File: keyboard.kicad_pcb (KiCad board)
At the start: 2 copper layers, 129 parts, among them U1 MOUDLE-SEEEDUINO-XIAO

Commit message: Got everything placed
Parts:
- removed D67, D68, D69, D70: D0-35, onesemi-1N914:ON_Semiconductor-017AG-08_2016-O-MFG
- removed U1: MOUDLE-SEEEDUINO-XIAO, XIAO_PCB:MOUDLE14P-2.54-21X17.8MM
- added D60: D0-35, onesemi-1N914:ON_Semiconductor-017AG-08_2016-O-MFG, F.Cu at (319.1, 73.8)
- added D61: D0-35, onesemi-1N914:ON_Semiconductor-017AG-08_2016-O-MFG, F.Cu at (322.3, 73.8)
- added D62: DO-35, onesemi-1N914:ON_Semiconductor-017AG-08_2016-O-MFG, F.Cu at (269.1, 65.9)
- added D64: D0-35, onesemi-1N914:ON_Semiconductor-017AG-08_2016-O-MFG, F.Cu at (319.1, 65.9)
- D1: footprint onesemi-1N914:ON_Semiconductor-017AG-08_2016-O-MFG -> MCU_RaspberryPi_and_Boards:RPi_Pico_SMD_TH; moved to B.Cu
- D55: value DO-35 -> D0-35
- locked: renamed from ENC1; value PEC11L-4120K-S0020 -> locked
- locked: renamed from ENC3; value PEC11L-4120K-S0020 -> locked
- locked: renamed from ENC2; value PEC11L-4120K-S0020 -> locked
- moved D2 435.6 mm to (61.9, 73.8), turned to -90 degrees
- moved D3 432.6 mm to (65.1, 73.8), turned to -90 degrees
- moved D4 429.6 mm to (68.3, 73.8), turned to -90 degrees
- moved D5 426.6 mm to (71.4, 73.8), turned to -90 degrees
- moved D6 422.1 mm to (76.2, 73.8), turned to -90 degrees
- moved D7 419.2 mm to (79.4, 73.8), turned to -90 degrees
- moved D8 416.3 mm to (82.5, 73.8), turned to -90 degrees
- moved D9 411.9 mm to (87.3, 73.8), turned to -90 degrees
- moved D10 409.0 mm to (90.5, 73.8), turned to -90 degrees
- moved D11 406.2 mm to (93.7, 73.8), turned to -90 degrees
- moved D12 403.4 mm to (96.8, 73.8), turned to -90 degrees
- moved D13 400.7 mm to (100.0, 73.8), turned to -90 degrees
- moved D14 396.4 mm to (104.8, 73.8), turned to -90 degrees
- moved D15 393.7 mm to (108.0, 73.8), turned to -90 degrees
- moved D17 393.2 mm to (114.3, 73.8), turned to -90 degrees
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- renumbered MX42 to MX41, MX43 to MX42, MX45 to MX43, MX46 to MX44, MX47 to MX45, MX48 to MX46, MX49 to MX47, MX50 to MX48, MX51 to MX49, MX52 to MX50, MX53 to MX51, MX54 to MX52, MX56 to MX53, MX57 to MX54, MX58 to MX55, MX59 to MX56, MX63 to MX57, MX67 to MX58, MX68 to MX59, MX69 to MX60, MX70 to MX61
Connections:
- D10 pad 1: ROW0 -> ROW1
- D11 pad 1: ROW0 -> Net-(D11-K)
- D12 pad 1: ROW0 -> ROW3
- D13 pad 1: ROW0 -> ROW4
- D16 pad 1: ROW1 -> Net-(D11-K)
- D17 pad 1: ROW1 -> ROW3
- D18 pad 1: ROW1 -> ROW0
- D2 pad 1: ROW0 -> ROW1
- D20 pad 1: ROW1 -> Net-(D11-K)
- D21 pad 1: ROW1 -> ROW3
- D22 pad 1: ROW1 -> ROW0
- D24 pad 1: ROW1 -> Net-(D11-K)
- D25 pad 1: ROW1 -> ROW3
- D26 pad 1: ROW1 -> ROW0
- D28 pad 1: ROW1 -> Net-(D11-K)
- D29 pad 1: ROW2 -> ROW3
- D3 pad 1: ROW0 -> ROW2
- D30 pad 1: ROW2 -> ROW0
- D31 pad 1: ROW2 -> ROW1
- D32 pad 1: ROW2 -> Net-(D11-K)
- D33 pad 1: ROW2 -> ROW3
- D34 pad 1: ROW2 -> ROW4
- D35 pad 1: ROW2 -> ROW0
- D36 pad 1: ROW2 -> ROW1
- D37 pad 1: ROW2 -> Net-(D11-K)
- D38 pad 1: ROW2 -> ROW3
- D39 pad 1: ROW2 -> ROW0
- D4 pad 1: ROW0 -> ROW3
- D40 pad 1: ROW2 -> ROW1
- D41 pad 1: ROW0 -> Net-(D11-K)
- D42 pad 1: ROW2 -> ROW3
- D43 pad 1: ROW3 -> ROW0
- D44 pad 1: ROW0 -> ROW1
- D45 pad 1: ROW3 -> Net-(D11-K)
- D47 pad 1: ROW3 -> ROW4
- D48 pad 1: ROW3 -> ROW0
- D49 pad 1: ROW3 -> ROW1
- D5 pad 1: ROW0 -> ROW4
- D50 pad 1: ROW3 -> Net-(D11-K)
- D52 pad 1: ROW3 -> ROW4
- D53 pad 1: ROW3 -> ROW0
- D54 pad 1: ROW3 -> ROW1
- D55 pad 1: ROW0 -> Net-(D11-K)
- D56 pad 1: ROW3 -> ROW4
- D57 pad 1: ROW4 -> ROW0
- D58 pad 1: ROW4 -> ROW1
- D59 pad 1: ROW4 -> Net-(D11-K)
- D63 pad 1: ROW4 -> ROW0
- D7 pad 1: ROW0 -> ROW1
- D8 pad 1: ROW0 -> ROW4
- MX10 pad 2: Net-(D10-A) -> Net-(D39-A)
- MX11 pad 2: Net-(D11-A) -> Net-(D43-A)
- MX12 pad 2: Net-(D12-A) -> Net-(D48-A)
- MX13 pad 2: Net-(D13-A) -> Net-(D53-A)
- MX14 pad 2: Net-(D14-A) -> Net-(D57-A)
- MX15 pad 2: Net-(D15-A) -> Net-(D2-A)
- MX16 pad 2: Net-(D16-A) -> Net-(D7-A)
- MX17 pad 2: Net-(D17-A) -> Net-(D10-A)
- MX18 pad 2: Net-(D18-A) -> Net-(D15-A)
- MX2 pad 2: Net-(D2-A) -> Net-(D6-A)
- MX20 pad 2: Net-(D20-A) -> Net-(D23-A)
- MX21 pad 2: Net-(D21-A) -> Net-(D27-A)
- MX22 pad 2: Net-(D22-A) -> Net-(D31-A)
- MX23 pad 2: Net-(D23-A) -> Net-(D36-A)
- MX24 pad 2: Net-(D24-A) -> Net-(D40-A)
- MX25 pad 2: Net-(D25-A) -> Net-(D44-A)
- MX26 pad 2: Net-(D26-A) -> Net-(D49-A)
- MX27 pad 2: Net-(D27-A) -> Net-(D54-A)
- MX28 pad 2: Net-(D28-A) -> Net-(D58-A)
- MX29 pad 2: Net-(D29-A) -> Net-(D3-A)
- MX3 pad 2: Net-(D3-A) -> Net-(D9-A)
- MX30 pad 1: COL1 -> COL2
- MX30 pad 2: Net-(D30-A) -> Net-(D11-A)
- MX31 pad 2: Net-(D31-A) -> Net-(D16-A)
- MX32 pad 2: Net-(D32-A) -> Net-(D20-A)
- MX33 pad 2: Net-(D33-A) -> Net-(D24-A)
- MX34 pad 2: Net-(D34-A) -> Net-(D28-A)
- MX35 pad 2: Net-(D35-A) -> Net-(D32-A)
- MX36 pad 2: Net-(D36-A) -> Net-(D37-A)
- MX37 pad 2: Net-(D37-A) -> Net-(D41-A)
- MX38 pad 2: Net-(D38-A) -> Net-(D45-A)
- MX39 pad 2: Net-(D39-A) -> Net-(D50-A)
- MX4 pad 2: Net-(D4-A) -> Net-(D14-A)
- MX40 pad 1: ROW1 -> COL12
- MX40 pad 2: Net-(D40-A) -> Net-(D55-A)
- MX41 pad 2: Net-(D42-A) -> Net-(D59-A)
- MX42 pad 2: Net-(D43-A) -> Net-(D4-A)
- MX43 pad 1: COl3 -> COL2
- MX43 pad 2: Net-(D45-A) -> Net-(D12-A)
- MX44 pad 1: COl4 -> COl3
- MX44 pad 2: Net-(D46-A) -> Net-(D17-A)
- MX45 pad 1: COL5 -> COl4
- MX45 pad 2: Net-(D47-A) -> Net-(D21-A)
- MX46 pad 1: COL6 -> COL5
- MX46 pad 2: Net-(D48-A) -> Net-(D25-A)
- MX47 pad 1: COL7 -> COL6
- MX47 pad 2: Net-(D49-A) -> Net-(D29-A)
- MX48 pad 1: COL8 -> COL7
- MX48 pad 2: Net-(D50-A) -> Net-(D33-A)
- MX49 pad 1: COL9 -> COL8
- MX49 pad 2: Net-(D51-A) -> Net-(D38-A)
- MX5 pad 2: Net-(D5-A) -> Net-(D18-A)
- MX50 pad 1: COL10 -> COL9
- MX50 pad 2: Net-(D52-A) -> Net-(D42-A)
- MX51 pad 1: COL11 -> COL10
- MX51 pad 2: Net-(D53-A) -> Net-(D46-A)
- MX52 pad 1: ROW2 -> COL11
- MX52 pad 2: Net-(D54-A) -> Net-(D51-A)
- MX53 pad 2: Net-(D56-A) -> Net-(D60-A)
- MX54 pad 2: Net-(D57-A) -> Net-(D5-A)
- MX55 pad 2: Net-(D58-A) -> Net-(D8-A)
- MX56 pad 2: Net-(D59-A) -> Net-(D13-A)
- MX57 pad 1: COL8 -> COL7
- MX57 pad 2: Net-(D63-A) -> Net-(D34-A)
- MX58 pad 2: Net-(D67-A) -> Net-(D47-A)
- MX59 pad 2: Net-(D68-A) -> Net-(D52-A)
- MX6 pad 2: Net-(D6-A) -> Net-(D22-A)
- MX60 pad 1: ROW2 -> COL12
- MX60 pad 2: Net-(D69-A) -> Net-(D56-A)
- MX7 pad 2: Net-(D7-A) -> Net-(D26-A)
- MX8 pad 2: Net-(D8-A) -> Net-(D30-A)
- MX9 pad 2: Net-(D9-A) -> Net-(D35-A)
- locked pad 2: Net-(D41-A) -> Net-(D64-A)
- locked pad 1: COL10 -> COL11
- locked pad 2: Net-(D55-A) -> Net-(D62-A)
- locked pad 2: Net-(D44-A) -> Net-(D63-A)
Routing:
- net COL7: track 0.00 -> 93.9 mm
- net Net-(D5-A): track 0.00 -> 92.9 mm
- net COL12: track 0.00 -> 92.1 mm
- net COl3: track 0.00 -> 90.9 mm
- net Net-(D8-A): track 0.00 -> 89.1 mm
- net COL11: track 0.00 -> 87.2 mm
- net COL10: track 0.00 -> 86.1 mm
- net COL13: track 0.00 -> 84.1 mm
- net COL0: track 0.00 -> 83.1 mm
- net COL1: track 0.00 -> 81.9 mm
- net COl4: track 0.00 -> 69.0 mm
- net COL5: track 0.00 -> 69.0 mm
- net COL6: track 0.00 -> 69.0 mm
- net COL2: track 0.00 -> 69.0 mm
- net COL9: track 0.00 -> 68.0 mm
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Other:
- board outline added: 285.8 x 125.4 mm

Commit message: forgot to save
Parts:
- added U1: Pi Pico, MCU_RaspberryPi_and_Boards:RPi_Pico_SMD_TH, B.Cu at (198.4, 75.4)
- D1: value D0-35 -> DO-35; footprint MCU_RaspberryPi_and_Boards:RPi_Pico_SMD_TH -> onesemi-1N914:ON_Semiconductor-017AG-08_2016-O-MFG; moved to F.Cu
- moved D1 139.7 mm to (58.7, 73.8), turned to -90 degrees

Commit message: Routed diodes to switches
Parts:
- D1: value DO-35 -> PI Pico
- U1: value Pi Pico -> Pico
- moved D17 14.3 mm to (114.3, 73.8)
- moved D13 3.18 mm to (101.6, 73.8)
- moved D14 3.17 mm to (104.8, 73.8)
- moved D15 3.17 mm to (108.0, 73.8)
- moved D16 3.17 mm to (111.1, 73.8)
- renumbered D14 to D13, D15 to D14, D16 to D15, D17 to D16, D13 to D17
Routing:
- net Net-(D34-A): track 0.00 -> 132.6 mm
- net Net-(D52-A): track 0.00 -> 113.2 mm
- net Net-(D17-A): track 0.00 -> 111.6 mm
- net Net-(D47-A): track 0.00 -> 110.8 mm
- net Net-(D33-A): track 0.00 -> 109.6 mm
- net Net-(D56-A): track 0.00 -> 102.5 mm
- net Net-(D29-A): track 0.00 -> 100.6 mm
- net Net-(D32-A): track 0.00 -> 96.6 mm
- net Net-(D61-A): track 0.00 -> 95.2 mm
- net Net-(D37-A): track 0.00 -> 93.9 mm
- net Net-(D25-A): track 0.00 -> 93.8 mm
- net Net-(D51-A): track 0.00 -> 93.6 mm
- net Net-(D46-A): track 0.00 -> 91.9 mm
- net Net-(D21-A): track 0.00 -> 90.5 mm
- net Net-(D16-A): track 0.00 -> 89.1 mm
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
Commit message: Tracing mostly done just do DRC
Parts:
- D2: moved to B.Cu
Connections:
- D11 pad 1: Net-(D11-K) -> ROW2
- D15 pad 1: Net-(D11-K) -> ROW2
- D20 pad 1: Net-(D11-K) -> ROW2
- D24 pad 1: Net-(D11-K) -> ROW2
- D28 pad 1: Net-(D11-K) -> ROW2
- D32 pad 1: Net-(D11-K) -> ROW2
- D37 pad 1: Net-(D11-K) -> ROW2
- D41 pad 1: Net-(D11-K) -> ROW2
- D45 pad 1: Net-(D11-K) -> ROW2
- D50 pad 1: Net-(D11-K) -> ROW2
- D55 pad 1: Net-(D11-K) -> ROW2
- D59 pad 1: Net-(D11-K) -> ROW2
- MX18 pad 1: COl3 -> COL3
- MX19 pad 1: COl4 -> COL4
- MX31 pad 1: COl3 -> COL3
- MX32 pad 1: COl4 -> COL4
- MX4 pad 1: COl3 -> COL3
- MX44 pad 1: COl3 -> COL3
- MX45 pad 1: COl4 -> COL4
- MX5 pad 1: COl4 -> COL4
- MX56 pad 1: COl3 -> COL3
- U1 pad 1: unconnected-(U1-GPIO0-Pad1) -> ENC3B
- U1 pad 10: unconnected-(U1-GPIO7-Pad10) -> ENC2A
- U1 pad 11: unconnected-(U1-GPIO8-Pad11) -> ENC1B
- U1 pad 12: unconnected-(U1-GPIO9-Pad12) -> ENC1A
- U1 pad 13: unconnected-(U1-GND-Pad13) -> GND
- U1 pad 14: unconnected-(U1-GPIO10-Pad14) -> COL8
- U1 pad 15: unconnected-(U1-GPIO11-Pad15) -> COL9
- U1 pad 16: unconnected-(U1-GPIO12-Pad16) -> COL10
- U1 pad 17: unconnected-(U1-GPIO13-Pad17) -> COL11
- U1 pad 18: unconnected-(U1-GND-Pad18) -> GND
- U1 pad 19: unconnected-(U1-GPIO14-Pad19) -> COL12
- U1 pad 2: unconnected-(U1-GPIO1-Pad2) -> ENC3A
- U1 pad 20: unconnected-(U1-GPIO15-Pad20) -> COL13
- U1 pad 21: unconnected-(U1-GPIO16-Pad21) -> COL2
- U1 pad 22: unconnected-(U1-GPIO17-Pad22) -> COL3
- U1 pad 23: unconnected-(U1-GND-Pad23) -> GND
- U1 pad 24: unconnected-(U1-GPIO18-Pad24) -> COL4
- U1 pad 25: unconnected-(U1-GPIO19-Pad25) -> COL5
- U1 pad 26: unconnected-(U1-GPIO20-Pad26) -> COL6
- U1 pad 27: unconnected-(U1-GPIO21-Pad27) -> COL7
- U1 pad 28: unconnected-(U1-GND-Pad28) -> GND
- U1 pad 29: unconnected-(U1-GPIO22-Pad29) -> COL1
- U1 pad 3: unconnected-(U1-GND-Pad3) -> GND
- U1 pad 31: unconnected-(U1-GPIO26_ADC0-Pad31) -> COL0
- U1 pad 34: unconnected-(U1-GPIO28_ADC2-Pad34) -> ROW0
- U1 pad 38: unconnected-(U1-GND-Pad38) -> GND
- U1 pad 4: unconnected-(U1-GPIO2-Pad4) -> ROW4
- U1 pad 5: unconnected-(U1-GPIO3-Pad5) -> ROW3
- U1 pad 6: unconnected-(U1-GPIO4-Pad6) -> ROW2
- U1 pad 7: unconnected-(U1-GPIO5-Pad7) -> ROW1
- U1 pad 8: unconnected-(U1-GND-Pad8) -> GND
- U1 pad 9: unconnected-(U1-GPIO6-Pad9) -> ENC2B
- locked pad A: unconnected-(ENC3-CHANNEL_A-PadA) -> ENC3A
- locked pad B: unconnected-(ENC3-CHANNEL_B-PadB) -> ENC3B
- locked pad C: unconnected-(ENC3-COMMON-PadC) -> GND
- locked pad A: unconnected-(ENC1-CHANNEL_A-PadA) -> ENC1A
- locked pad B: unconnected-(ENC1-CHANNEL_B-PadB) -> ENC1B
- locked pad C: unconnected-(ENC1-COMMON-PadC) -> GND
- locked pad A: unconnected-(ENC2-CHANNEL_A-PadA) -> ENC2A
- locked pad B: unconnected-(ENC2-CHANNEL_B-PadB) -> ENC2B
- locked pad C: unconnected-(ENC2-COMMON-PadC) -> GND
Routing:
- net ROW3: track 0.00 -> 319.1 mm, vias 0 -> 12
- net ROW2: track 0.00 -> 313.6 mm, vias 0 -> 12
- net ROW4: track 0.00 -> 313.3 mm, vias 0 -> 8
- net ROW0: track 0.00 -> 288.4 mm, vias 0 -> 3
- net ROW1: track 0.00 -> 275.2 mm, vias 0 -> 13
- net GND: track 0.00 -> 171.9 mm, vias 0 -> 6
- net COL3: track 0.00 -> 166.5 mm
- net ENC3B: track 0.00 -> 149.4 mm
- net ENC3A: track 0.00 -> 146.7 mm
- net COL0: track 83.1 -> 214.8 mm
- net ENC2A: track 0.00 -> 128.3 mm
- net ENC2B: track 0.00 -> 128.2 mm
- net COL4: track 0.00 -> 123.3 mm
- net COL13: track 109.3 -> 225.9 mm
- net COL1: track 81.9 -> 192.1 mm
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
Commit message: Should be completely done
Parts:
- added ?: , , F.Cu at (95.2, 93.7)
- added REF**: MountingHoleM2-5mmby2mm, MountingHoles:MountingHoleM2-5mmby2mm, F.Cu at (83.3, 108.0)
- added REF**: MountingHoleM2-5mmby2mm, MountingHoles:MountingHoleM2-5mmby2mm, F.Cu at (315.1, 108.0)
- added REF**: MountingHoleM2-5mmby2mm, MountingHoles:MountingHoleM2-5mmby2mm, F.Cu at (95.2, 93.7)
- added REF**: MountingHoleM2-5mmby2mm, MountingHoles:MountingHoleM2-5mmby2mm, F.Cu at (304.8, 91.3)
- added REF**: MountingHoleM2-5mmby2mm, MountingHoles:MountingHoleM2-5mmby2mm, F.Cu at (96.8, 146.1)
- added REF**: MountingHoleM2-5mmby2mm, MountingHoles:MountingHoleM2-5mmby2mm, F.Cu at (191.3, 115.9)
- added REF**: MountingHoleM2-5mmby2mm, MountingHoles:MountingHoleM2-5mmby2mm, F.Cu at (293.7, 146.1)
- D2: moved to F.Cu
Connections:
- U1 pad 13: GND -> unconnected-(U1-GND-Pad13)
- U1 pad 23: GND -> unconnected-(U1-GND-Pad23)
- U1 pad 28: GND -> unconnected-(U1-GND-Pad28)
- U1 pad 3: GND -> unconnected-(U1-GND-Pad3)
- U1 pad 38: GND -> unconnected-(U1-GND-Pad38)
- U1 pad 8: GND -> unconnected-(U1-GND-Pad8)
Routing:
- net ROW2: track 313.6 -> 318.1 mm, vias 12 -> 13
- net ROW1: track 275.2 -> 278.1 mm, vias 13 -> 14
- net ROW0: track 288.4 -> 290.1 mm
- net COL10: track 135.0 -> 133.9 mm
- net GND: track 171.9 -> 172.9 mm
- net COL12: track 208.1 -> 207.2 mm

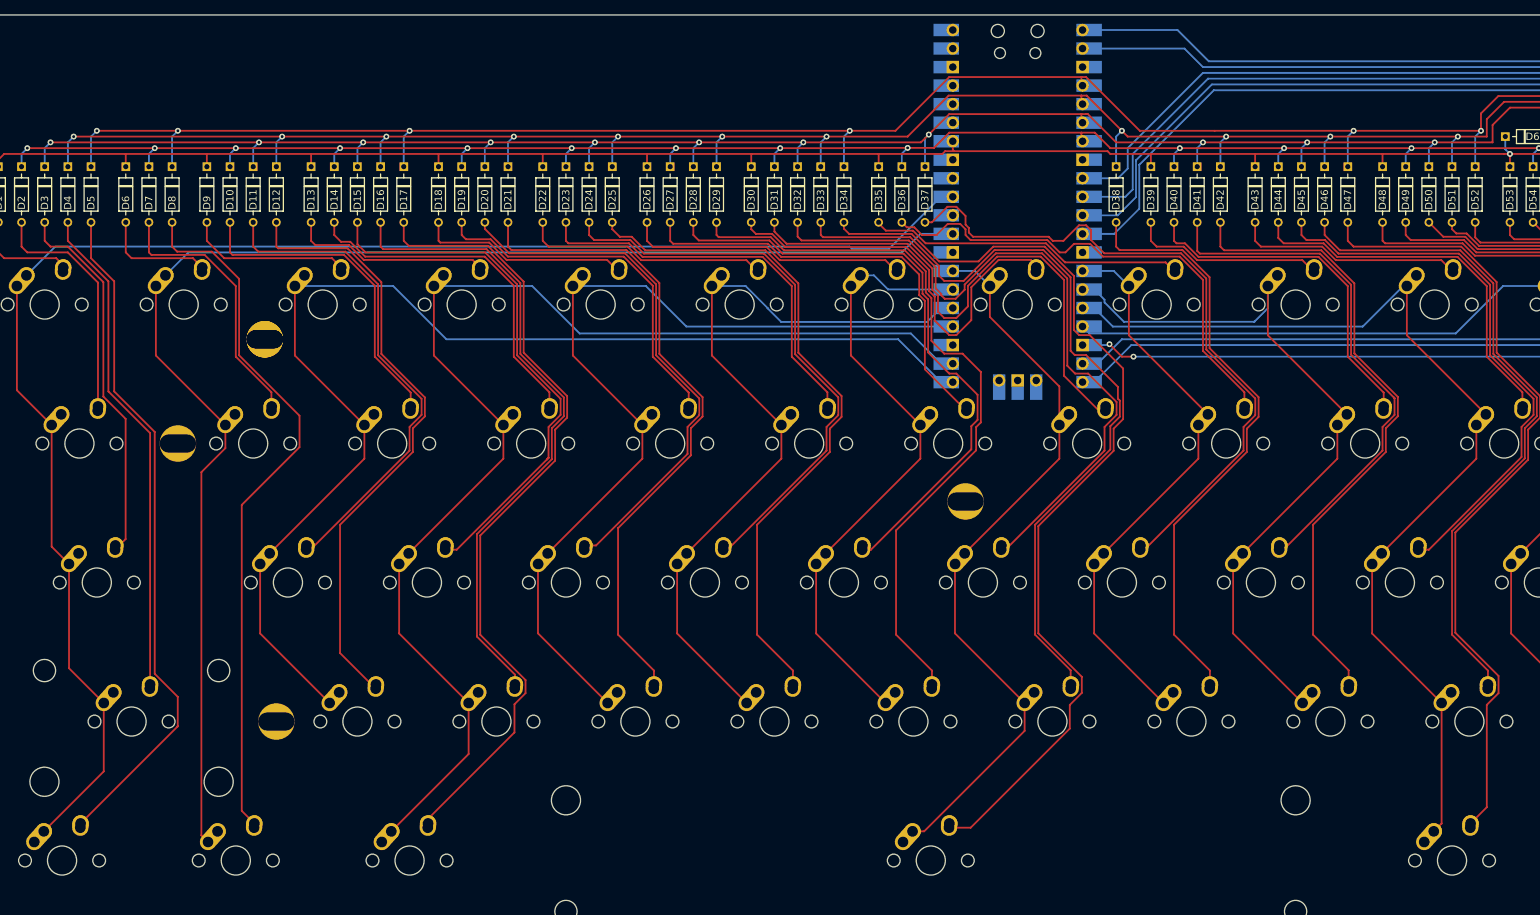
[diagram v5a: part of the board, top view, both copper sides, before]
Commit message: With brakeouts
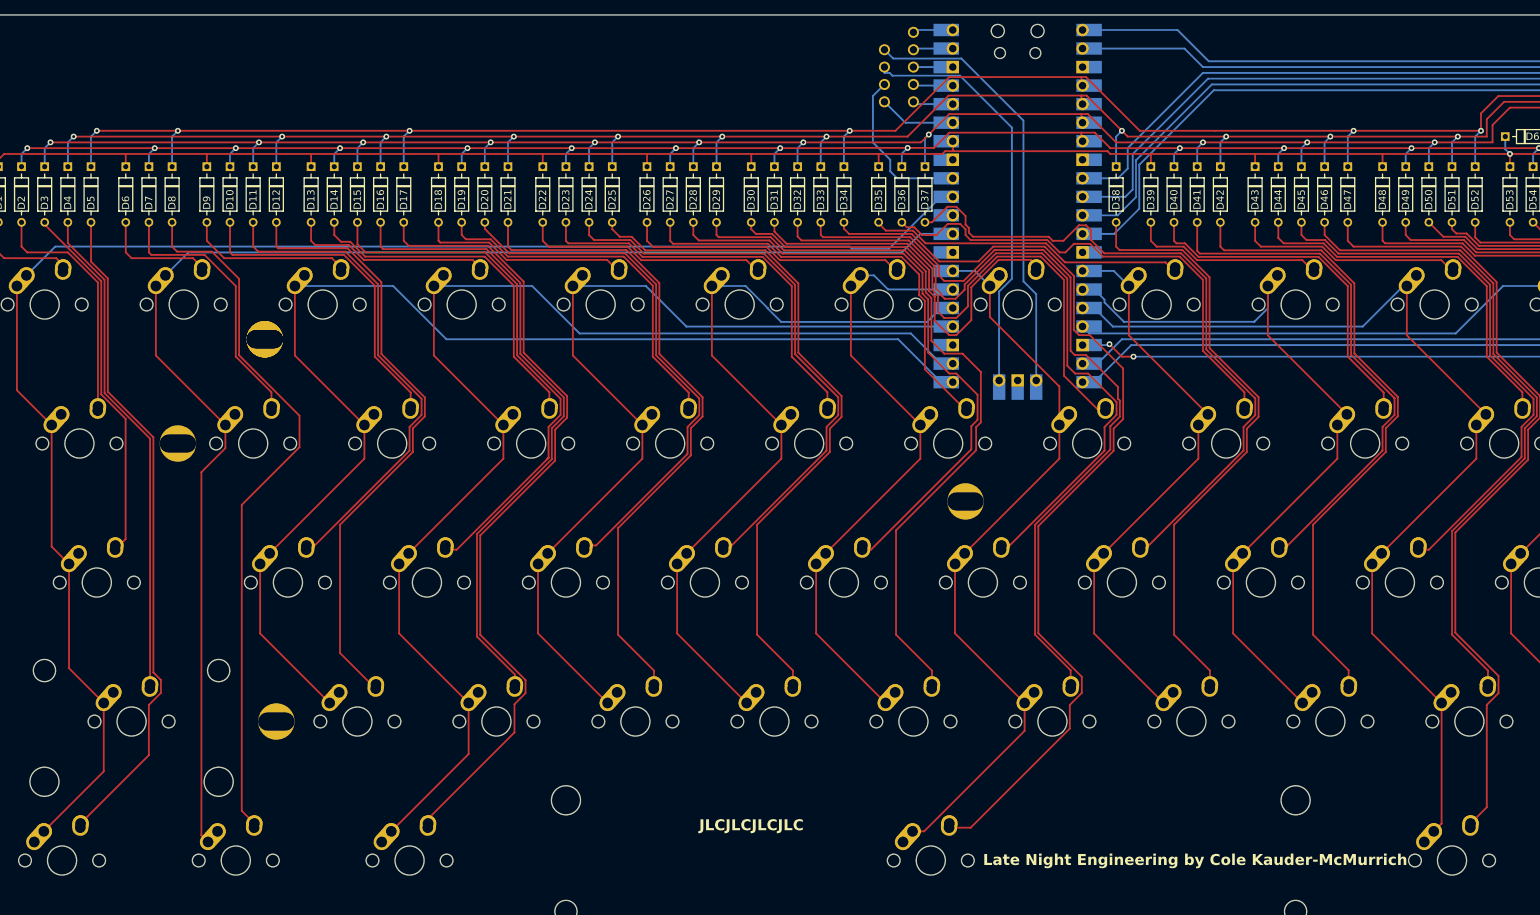
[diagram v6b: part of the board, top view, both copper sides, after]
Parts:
- added Hole1: ~, MountingHoles:Holes, F.Cu at (184.1, 51.6)
- added Hole2: ~, MountingHoles:Holes, F.Cu at (184.1, 58.7)
- added Hole3: ~, MountingHoles:Holes, F.Cu at (184.1, 56.4)
- added Hole4: ~, MountingHoles:Holes, F.Cu at (184.1, 54.0)
- added Hole5: ~, MountingHoles:Holes, F.Cu at (180.2, 61.1)
- added Hole6: ~, MountingHoles:Holes, F.Cu at (180.2, 58.7)
- added Hole7: ~, MountingHoles:Holes, F.Cu at (184.1, 61.1)
- added Hole8: ~, MountingHoles:Holes, F.Cu at (180.2, 54.0)
- added Hole9: ~, MountingHoles:Holes, F.Cu at (180.2, 56.4)
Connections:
- U1 pad 32: unconnected-(U1-GPIO27_ADC1-Pad32) -> Net-(U1-GPIO27_ADC1)
- U1 pad 35: unconnected-(U1-ADC_VREF-Pad35) -> Net-(U1-ADC_VREF)
- U1 pad 36: unconnected-(U1-3V3-Pad36) -> Net-(U1-3V3)
- U1 pad 37: unconnected-(U1-3V3_EN-Pad37) -> Net-(U1-3V3_EN)
- U1 pad 38: unconnected-(U1-GND-Pad38) -> Net-(Hole3-Pad)
- U1 pad 39: unconnected-(U1-VSYS-Pad39) -> Net-(U1-VSYS)
- U1 pad 40: unconnected-(U1-VBUS-Pad40) -> Net-(U1-VBUS)
- U1 pad 41: unconnected-(U1-SWCLK-Pad41) -> Net-(U1-SWCLK)
- U1 pad 43: unconnected-(U1-SWDIO-Pad43) -> Net-(U1-SWDIO)
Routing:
- net Net-(U1-SWCLK): track 0.00 -> 59.4 mm
- net Net-(U1-SWDIO): track 0.00 -> 56.7 mm
- net Net-(U1-GPIO27_ADC1): track 0.00 -> 22.5 mm
- net Net-(U1-ADC_VREF): track 0.00 -> 10.5 mm
- net Net-(U1-VBUS): track 0.00 -> 5.53 mm
- net Net-(U1-3V3): track 0.00 -> 5.53 mm
- net Net-(U1-VSYS): track 0.00 -> 5.46 mm
- net Net-(U1-3V3_EN): track 0.00 -> 5.46 mm
- net Net-(Hole3-Pad): track 0.00 -> 5.40 mm
- net Net-(D5-A): track 92.9 -> 90.9 mm
- net Net-(D3-A): track 51.5 -> 50.1 mm
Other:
- board text added: "JLCJLCJLCJLC"
- board text added: "Late Night Engineering by Cole Kauder-McMurrich"

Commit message: Remove brakouts
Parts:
- removed Hole1, Hole2, Hole3, Hole4, Hole5, Hole6, Hole7, Hole8, Hole9: ~, MountingHoles:Holes
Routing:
- net Net-(U1-SWCLK): track 59.4 -> 0.00 mm
- net Net-(U1-SWDIO): track 56.7 -> 0.00 mm
- net Net-(U1-GPIO27_ADC1): track 22.5 -> 0.00 mm
- net Net-(U1-ADC_VREF): track 10.5 -> 0.00 mm
- net Net-(U1-VBUS): track 5.53 -> 0.00 mm
- net Net-(U1-3V3): track 5.53 -> 0.00 mm
- net Net-(U1-VSYS): track 5.46 -> 0.00 mm
- net Net-(U1-3V3_EN): track 5.46 -> 0.00 mm
- net Net-(Hole3-Pad): track 5.40 -> 0.00 mm
